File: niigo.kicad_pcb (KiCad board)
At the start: 2 copper layers, 53.4 x 61.4 mm, 7 parts, among them Q1 BC547, SW1 SW_Push

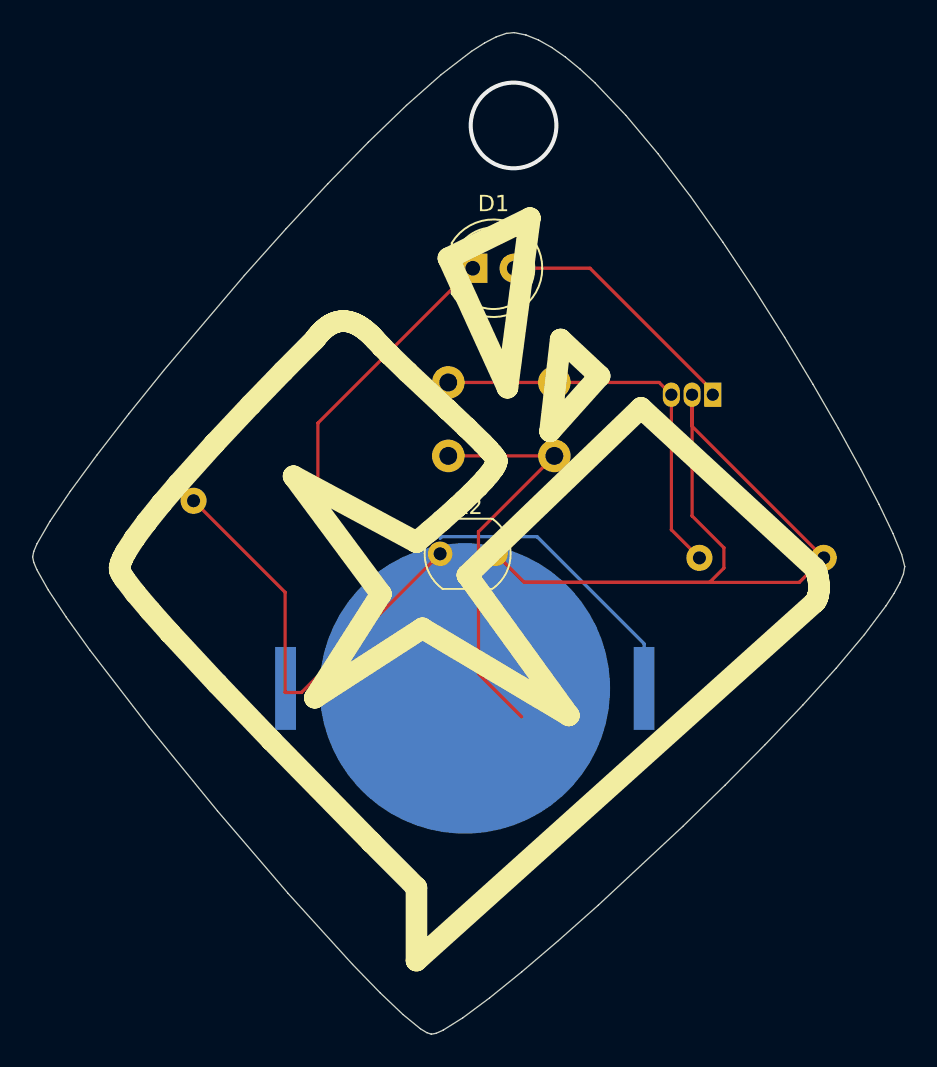
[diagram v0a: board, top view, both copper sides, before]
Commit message: v2.0 (+ .gbr and .srl files!)
v2.0 adds a vibrating motor with the motor disc given in the set (and more resistors...) and the gerbel and drill files needed for submission have been uploaded!
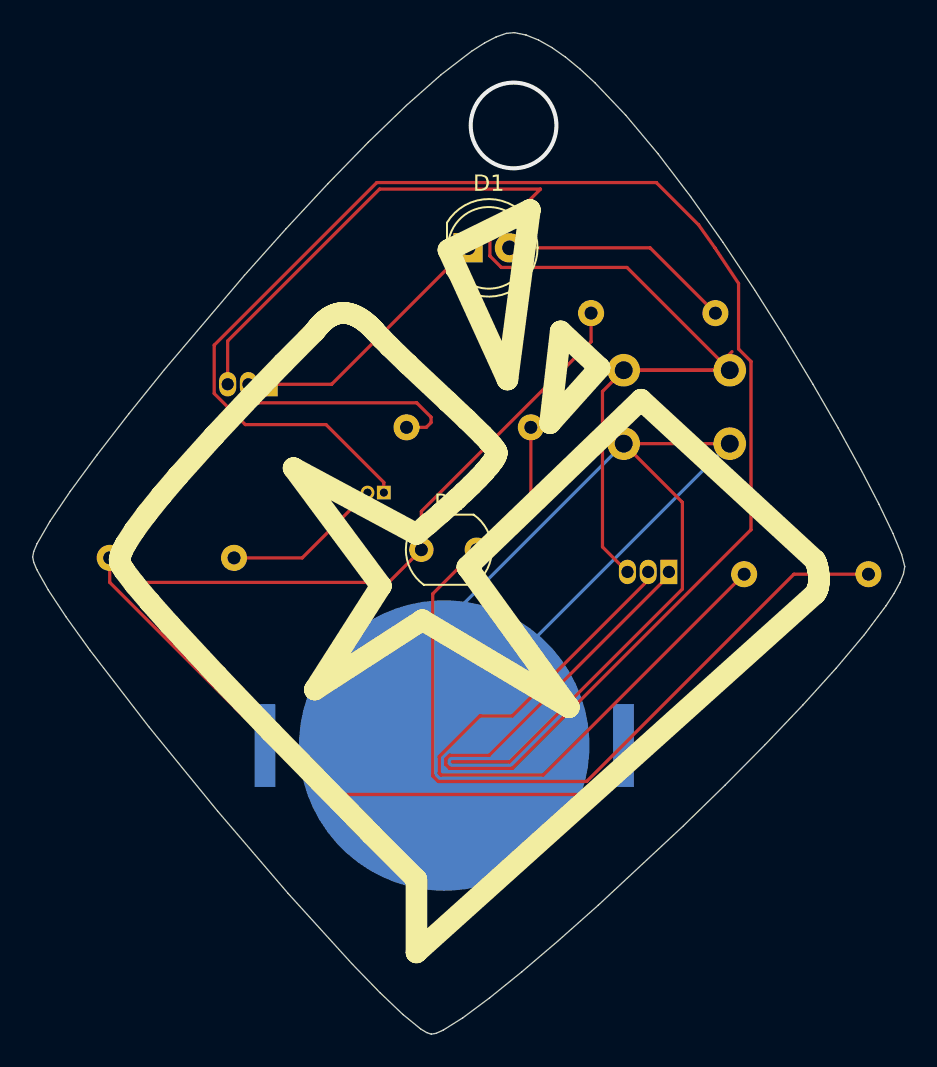
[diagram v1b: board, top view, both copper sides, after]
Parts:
- added M1: Motor_DC, Connector_PinHeader_1.00mm:PinHeader_2x01_P1.00mm_Horizontal, B.Cu at (222.8, 65.5)
- added Q2: BC547, Package_TO_SOT_THT:TO-92_Inline, B.Cu at (240.3, 70.4)
- added R4: 4.7K, Resistor_THT:R_Axial_DIN0207_L6.3mm_D2.5mm_P7.62mm_Horizontal, B.Cu at (213.6, 69.5)
- added R5: 4.7K, Resistor_THT:R_Axial_DIN0207_L6.3mm_D2.5mm_P7.62mm_Horizontal, B.Cu at (231.8, 61.5)
- R1: value R -> 4.7K
- R3: value R -> 470R
- moved Q1 27.2 mm to (215.8, 58.9)
- moved R3 26.9 mm to (243.1, 54.5)
- moved SW1 10.8 mm to (244.0, 58.0)
- moved BT1 3.72 mm to (226.5, 81.0)
- moved R1 2.92 mm to (252.5, 70.5)
- moved D1 1.28 mm to (228.0, 50.5)
- moved R2 1.18 mm to (225.1, 69.0)
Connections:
- Q1 pad 1: Net-(D1-A) -> Net-(D1-K)
- R1 pad 1: Net-(Q1-B) -> Net-(R1-Pad1)
- R1 pad 2: Net-(Q1-E) -> Net-(Q2-B)
- R2 pad 2: Net-(Q1-B) -> Net-(R1-Pad1)
- R3 pad 1: Net-(D1-K) -> Net-(D1-A)
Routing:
- net Net-(M1-+): track 0.00 -> 114.6 mm
- net Net-(BT1--): track 25.5 -> 86.4 mm
- net Net-(R1-Pad1): track 0.00 -> 56.0 mm
- net Net-(Q1-E): track 25.9 -> 75.8 mm
- net Net-(Q1-B): track 58.8 -> 14.3 mm
- net Net-(Q2-B): track 0.00 -> 42.6 mm
- net Net-(BT1-+): track 45.1 -> 78.8 mm
- net Net-(M1--): track 0.00 -> 9.84 mm
- net Net-(D1-K): track 18.2 -> 15.7 mm
- net Net-(D1-A): track 15.5 -> 14.3 mm
